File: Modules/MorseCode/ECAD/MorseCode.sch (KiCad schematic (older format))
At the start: 20 parts, among them J1 comm_header, J2 prog_header, SW1 Left, SW2 Right, SW3 Submit, U1 ATmega328-PU, U2 KCSC02-105, U3 KCSC02-105, U4 MAX7219, U5 KCSC02-105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

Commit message: Added polyfuses to all modules
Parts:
- added F1: Polyfuse, symbol Device:Polyfuse
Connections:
- net labels added: UVCC
- wire segments 126 -> 128
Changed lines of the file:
@@
 EESchema Schematic File Version 4
 LIBS:MorseCode-cache
-LIBS:Memory-cache
 EELAYER 29 0
 EELAYER END
@@
 L power:VCC #PWR01
 U 1 1 5F5DC5B2
-P 1400 3350
-F 0 "#PWR01" H 1400 3200 50  0001 C CNN
-F 1 "VCC" V 1418 3477 50  0000 L CNN
-F 2 "" H 1400 3350 50  0001 C CNN
-F 3 "" H 1400 3350 50  0001 C CNN
-	1    1400 3350
-	0    -1   -1   0
-$EndComp
-$Comp
-L power:VCC #PWR03
-U 1 1 5F5DD568
-P 1400 3950
-F 0 "#PWR03" H 1400 3800 50  0001 C CNN
-F 1 "VCC" V 1418 4077 50  0000 L CNN
-F 2 "" H 1400 3950 50  0001 C CNN
-F 3 "" H 1400 3950 50  0001 C CNN
-	1    1400 3950
-	0    -1   -1   0
+P 2250 3050
+F 0 "#PWR01" H 2250 2900 50  0001 C CNN
+F 1 "VCC" V 2268 3177 50  0000 L CNN
+F 2 "" H 2250 3050 50  0001 C CNN
+F 3 "" H 2250 3050 50  0001 C CNN
+	1    2250 3050
+	0    1    1    0
 $EndComp
 $Comp
@@
 Wire Wire Line
 	4850 2450 4400 2450
+$Comp
+L Device:Polyfuse F1
+U 1 1 5F923195
+P 2000 3050
+F 0 "F1" V 1775 3050 50  0000 C CNN
+F 1 "Polyfuse" V 1866 3050 50  0000 C CNN
+F 2 "" H 2050 2850 50  0001 L CNN
+F 3 "~" H 2000 3050 50  0001 C CNN
+	1    2000 3050
+	0    1    1    0
+$EndComp
+Text Label 1400 3950 2    50   ~ 0
+UVCC
+Text Label 1400 3350 2    50   ~ 0
+UVCC
+Text Label 1750 3050 2    50   ~ 0
+UVCC
+Wire Wire Line
+	1750 3050 1850 3050
+Wire Wire Line
+	2150 3050 2250 3050
 $EndSCHEMATC

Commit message: KiCad version update
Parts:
- U1: symbol MCU_Microchip_ATmega:ATmega328-PU -> MorseCode-rescue:ATmega328-PU-MCU_Microchip_ATmega
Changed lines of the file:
@@
 EESchema Schematic File Version 4
-LIBS:MorseCode-cache
-EELAYER 29 0
+EELAYER 30 0
 EELAYER END
 $Descr A4 11693 8268
@@
 $EndDescr
 $Comp
-L MCU_Microchip_ATmega:ATmega328-PU U1
+L MorseCode-rescue:ATmega328-PU-MCU_Microchip_ATmega U1
 U 1 1 5F833469
 P 3800 3250

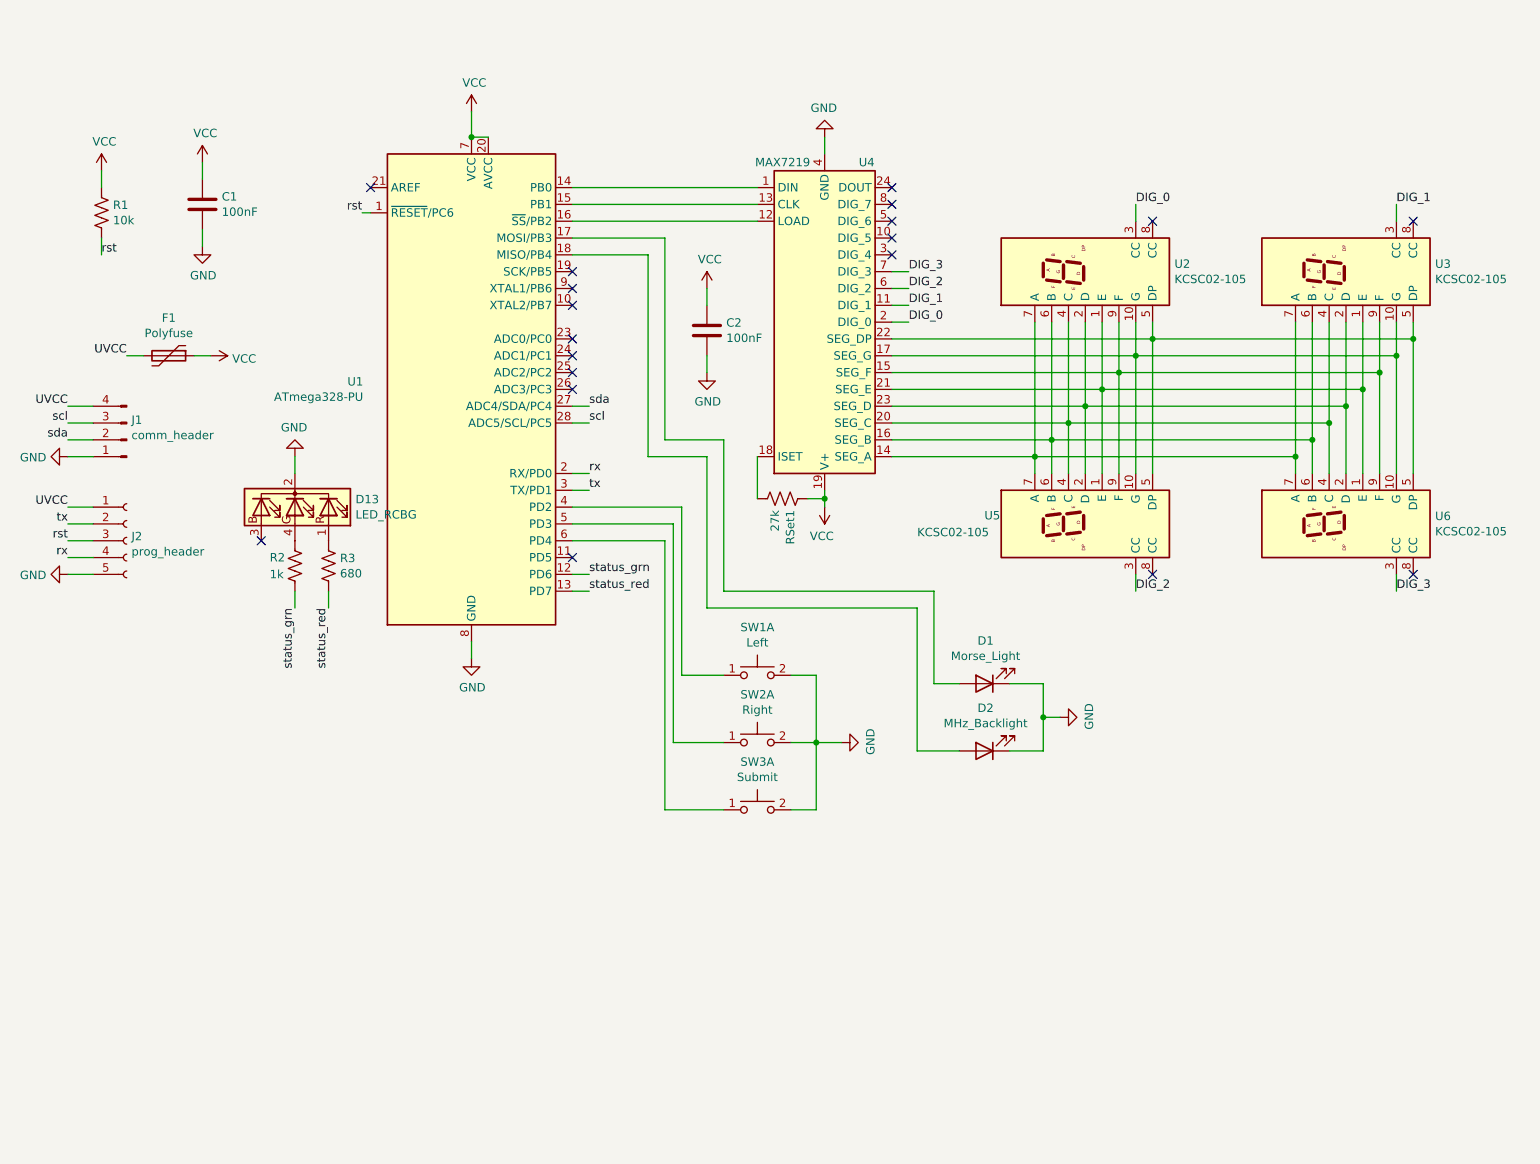
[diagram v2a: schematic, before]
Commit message: MorseCode: Added motor to schematic
This small motor will be used to show frequency with a physical marker
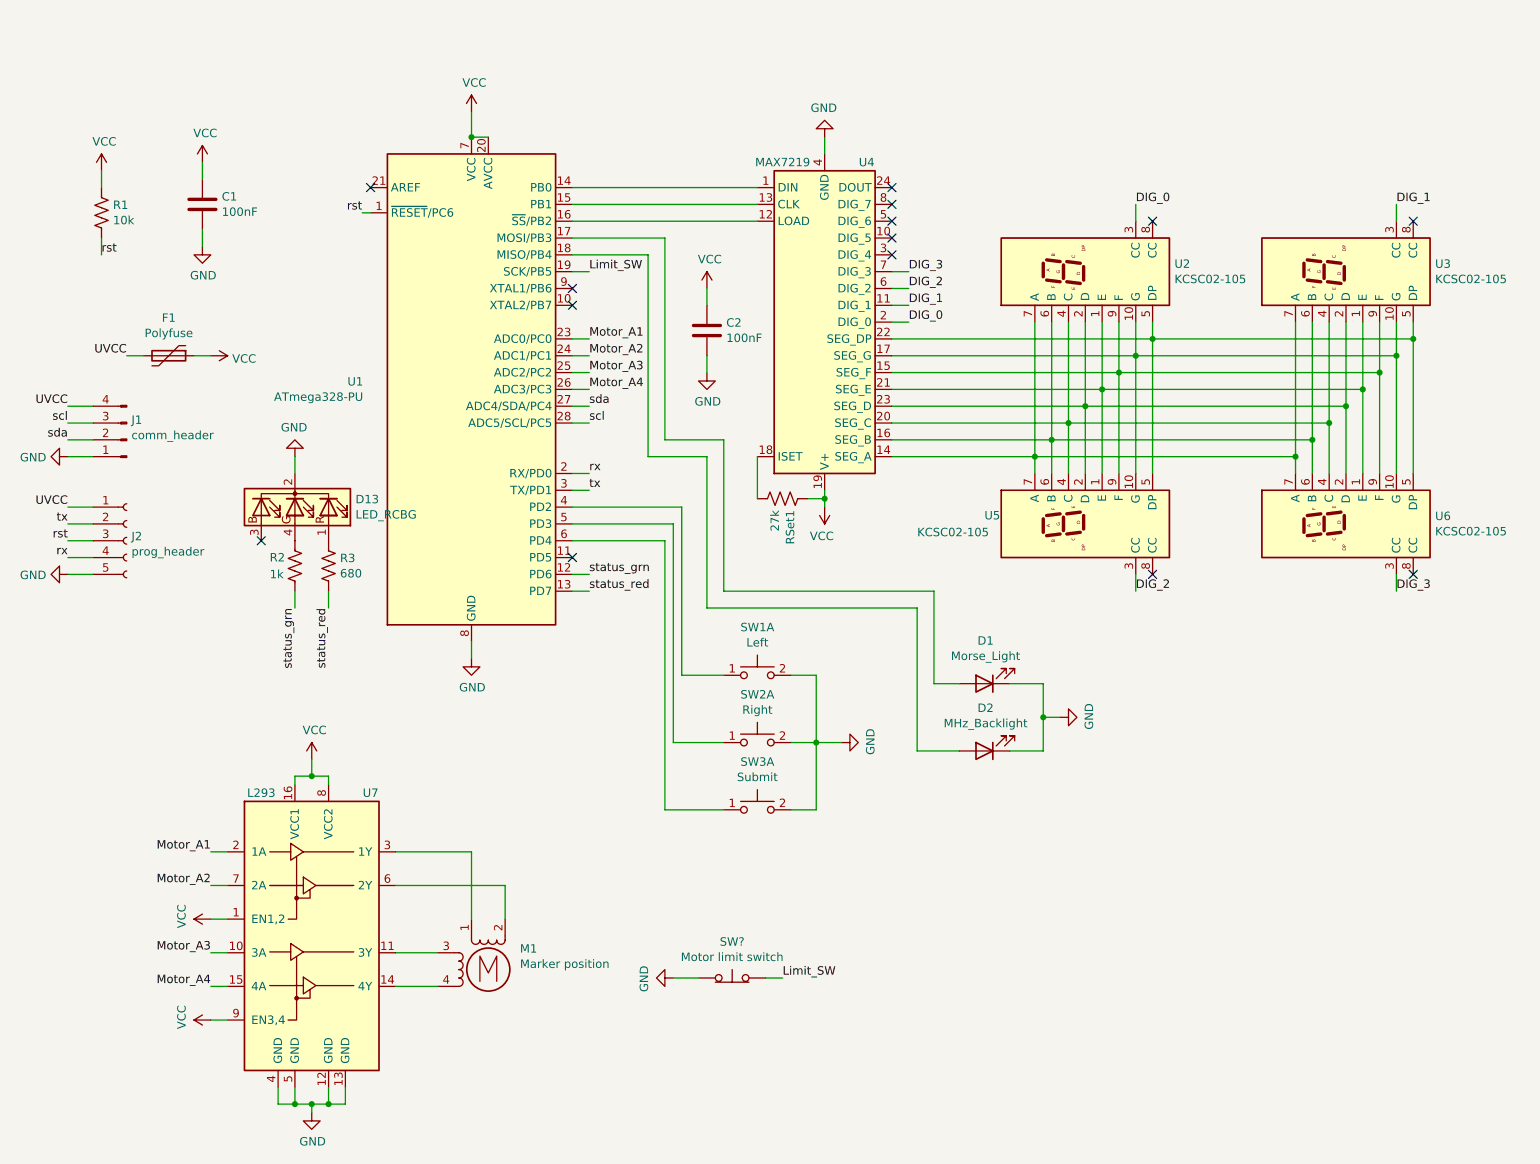
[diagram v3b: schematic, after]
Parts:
- added M1: Marker position, symbol Motor:Stepper_Motor_bipolar
- added SW?: Motor limit switch, symbol Switch:SW_Push_Open
- added U7: L293, Package_DIP:DIP-16_W7.62mm, symbol Driver_Motor:L293
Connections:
- net GND: now also SW?.1 (A), U7.12 (GND), U7.13 (GND), U7.4 (GND), U7.5 (GND)
- net VCC: now also U7.1 (EN1,2), U7.16 (VCC1), U7.8 (VCC2), U7.9 (EN3,4)
- net Limit_SW: now reaches U1.19 (SCK/PB5)
- net Limit_SW: now also SW?.2 (B)
- net Motor_A1: now reaches U1.23 (ADC0/PC0)
- net Motor_A1: now also U7.2 (1A)
- net Motor_A2: now reaches U1.24 (ADC1/PC1)
- net Motor_A2: now also U7.7 (2A)
- net Motor_A3: now reaches U1.25 (ADC2/PC2)
- net Motor_A3: now also U7.10 (3A)
- net Motor_A4: now reaches U1.26 (ADC3/PC3)
- net Motor_A4: now also U7.15 (4A)
- new net: M1.3, U7.11 (3Y)
- new net: M1.4, U7.14 (4Y)
- new net: M1.1, U7.3 (1Y)
- new net: M1.2 (-), U7.6 (2Y)
- no-connect marks 19 -> 14
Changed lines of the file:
@@
 Text Label 2950 4550 3    50   ~ 0
 status_red
-NoConn ~ 4400 2550
 NoConn ~ 4400 2650
 NoConn ~ 4400 2750
-NoConn ~ 4400 2950
-NoConn ~ 4400 3050
-NoConn ~ 4400 3150
-NoConn ~ 4400 3250
 $Comp
 L Device:R_US R2
@@
 Wire Wire Line
 	2150 3050 2250 3050
+$Comp
+L Driver_Motor:L293 U7
+U 1 1 60C7C92C
+P 2850 6600
+F 0 "U7" H 3200 7550 50  0000 C CNN
+F 1 "L293" H 2550 7550 50  0000 C CNN
+F 2 "Package_DIP:DIP-16_W7.62mm" H 3100 5850 50  0001 L CNN
+F 3 "http://www.ti.com/lit/ds/symlink/l293.pdf" H 2550 7300 50  0001 C CNN
+	1    2850 6600
+	1    0    0    -1
+$EndComp
+$Comp
+L power:GND #PWR019
+U 1 1 60C82B18
+P 2850 7550
+F 0 "#PWR019" H 2850 7300 50  0001 C CNN
+F 1 "GND" H 2855 7377 50  0000 C CNN
+F 2 "" H 2850 7550 50  0001 C CNN
+F 3 "" H 2850 7550 50  0001 C CNN
+	1    2850 7550
+	1    0    0    -1
+$EndComp
+$Comp
+L power:VCC #PWR018
+U 1 1 60C8344A
+P 2850 5450
+F 0 "#PWR018" H 2850 5300 50  0001 C CNN
+F 1 "VCC" H 2867 5623 50  0000 C CNN
+F 2 "" H 2850 5450 50  0001 C CNN
+F 3 "" H 2850 5450 50  0001 C CNN
+	1    2850 5450
+	1    0    0    -1
+$EndComp
+Wire Wire Line
+	2750 5600 2750 5550
+Wire Wire Line
+	2750 5550 2850 5550
+Wire Wire Line
+	2850 5550 2850 5450
+Wire Wire Line
+	2950 5600 2950 5550
+Wire Wire Line
+	2950 5550 2850 5550
+Connection ~ 2850 5550
+Wire Wire Line
+	2750 7400 2750 7500
+Wire Wire Line
+	2750 7500 2850 7500
+Wire Wire Line
+	2850 7500 2850 7550
+Wire Wire Line
+	2950 7400 2950 7500
+Wire Wire Line
+	2950 7500 2850 7500
+Connection ~ 2850 7500
+Wire Wire Line
+	3050 7400 3050 7500
+Wire Wire Line
+	3050 7500 2950 7500
+Connection ~ 2950 7500
+Wire Wire Line
+	2650 7400 2650 7500
+Wire Wire Line
+	2650 7500 2750 7500
+Connection ~ 2750 7500
+$Comp
+L Motor:Stepper_Motor_bipolar M1
+U 1 1 60CA94C4
+P 3900 6700
+F 0 "M1" H 4088 6824 50  0000 L CNN
+F 1 "Marker position" H 4088 6733 50  0000 L CNN
+F 2 "" H 3910 6690 50  0001 C CNN
+F 3 "http://www.infineon.com/dgdl/Application-Note-TLE8110EE_driving_UniPolarStepperMotor_V1.1.pdf?fileId=db3a30431be39b97011be5d0aa0a00b0" H 3910 6690 50  0001 C CNN
+	1    3900 6700
+	1    0    0    -1
+$EndComp
+Wire Wire Line
+	3350 6600 3600 6600
+Wire Wire Line
+	3600 6800 3350 6800
+Wire Wire Line
+	3350 6000 3800 6000
+Wire Wire Line
+	3800 6000 3800 6400
+Wire Wire Line
+	3350 6200 4000 6200
+Wire Wire Line
+	4000 6200 4000 6400
+Wire Wire Line
+	4500 2950 4400 2950
+Wire Wire Line
+	4500 3050 4400 3050
+Wire Wire Line
+	4500 3150 4400 3150
+Wire Wire Line
+	4500 3250 4400 3250
+Text Label 4500 2950 0    50   ~ 0
+Motor_A1
+Text Label 4500 3050 0    50   ~ 0
+Motor_A2
+Text Label 4500 3150 0    50   ~ 0
+Motor_A3
+Text Label 4500 3250 0    50   ~ 0
+Motor_A4
+Wire Wire Line
+	2250 6000 2350 6000
+Wire Wire Line
+	2250 6200 2350 6200
+Wire Wire Line
+	2250 6600 2350 6600
+Wire Wire Line
+	2250 6800 2350 6800
+Text Label 2250 6800 2    50   ~ 0
+Motor_A4
+Text Label 2250 6600 2    50   ~ 0
+Motor_A3
+Text Label 2250 6200 2    50   ~ 0
+Motor_A2
+Text Label 2250 6000 2    50   ~ 0
+Motor_A1
+$Comp
+L power:VCC #PWR017
+U 1 1 60D0045A
+P 2250 7000
+F 0 "#PWR017" H 2250 6850 50  0001 C CNN
+F 1 "VCC" H 2267 7173 50  0000 C CNN
+F 2 "" H 2250 7000 50  0001 C CNN
+F 3 "" H 2250 7000 50  0001 C CNN
+	1    2250 7000
+	0    -1   -1   0
+$EndComp
+$Comp
+L power:VCC #PWR03
+U 1 1 60D02180
+P 2250 6400
+F 0 "#PWR03" H 2250 6250 50  0001 C CNN
+F 1 "VCC" H 2267 6573 50  0000 C CNN
+F 2 "" H 2250 6400 50  0001 C CNN
+F 3 "" H 2250 6400 50  0001 C CNN
+	1    2250 6400
+	0    -1   -1   0
+$EndComp
+Wire Wire Line
+	2250 6400 2350 6400
+Wire Wire Line
+	2350 7000 2250 7000
+$Comp
+L Switch:SW_Push_Open SW?
+U 1 1 60D12947
+P 5350 6750
+F 0 "SW?" H 5350 6965 50  0000 C CNN
+F 1 "Motor limit switch" H 5350 6874 50  0000 C CNN
+F 2 "" H 5350 6950 50  0001 C CNN
+F 3 "~" H 5350 6950 50  0001 C CNN
+	1    5350 6750
+	1    0    0    -1
+$EndComp
+$Comp
+L power:GND #PWR?
+U 1 1 60D142A4
+P 5000 6750
+F 0 "#PWR?" H 5000 6500 50  0001 C CNN
+F 1 "GND" H 5005 6577 50  0000 C CNN
+F 2 "" H 5000 6750 50  0001 C CNN
+F 3 "" H 5000 6750 50  0001 C CNN
+	1    5000 6750
+	0    1    1    0
+$EndComp
+Wire Wire Line
+	5000 6750 5150 6750
+Wire Wire Line
+	5650 6750 5550 6750
+Text Label 5650 6750 0    50   ~ 0
+Limit_SW
+Text Label 4500 2550 0    50   ~ 0
+Limit_SW
+Wire Wire Line
+	4500 2550 4400 2550
 $EndSCHEMATC

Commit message: Update a bunch of stuff
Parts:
- removed SW?: Motor limit switch, symbol Switch:SW_Push_Open
- added R4: 10k, symbol Device:R_US
- added SW4: SW_Push_Dual, symbol Switch:SW_Push_Dual
- added SW5, SW6: SW_Push_SPDT, symbol Switch:SW_Push_SPDT
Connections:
- net GND: now also SW4.2, SW5.1 (A), SW6.1 (A)
- net Limit_SW: now also SW5.2 (B), SW6.2 (B)
- net VCC: now also R4.1, SW5.3 (C), SW6.3 (C); no longer U7.1 (EN1,2), U7.9 (EN3,4)
- net rst: now also SW4.1
- net Motor_EN: now reaches U1.11 (PD5)
- net Motor_EN: now also U7.1 (EN1,2), U7.9 (EN3,4), R4.2
- no-connect marks 14 -> 15
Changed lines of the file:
@@
 Wire Wire Line
 	4400 4150 4950 4150
-NoConn ~ 4400 4250
 $Comp
 L power:GND #PWR016
@@
 Text Label 2250 6000 2    50   ~ 0
 Motor_A1
-$Comp
-L power:VCC #PWR017
-U 1 1 60D0045A
-P 2250 7000
-F 0 "#PWR017" H 2250 6850 50  0001 C CNN
-F 1 "VCC" H 2267 7173 50  0000 C CNN
-F 2 "" H 2250 7000 50  0001 C CNN
-F 3 "" H 2250 7000 50  0001 C CNN
-	1    2250 7000
-	0    -1   -1   0
-$EndComp
-$Comp
-L power:VCC #PWR03
-U 1 1 60D02180
-P 2250 6400
-F 0 "#PWR03" H 2250 6250 50  0001 C CNN
-F 1 "VCC" H 2267 6573 50  0000 C CNN
-F 2 "" H 2250 6400 50  0001 C CNN
-F 3 "" H 2250 6400 50  0001 C CNN
-	1    2250 6400
-	0    -1   -1   0
-$EndComp
-Wire Wire Line
-	2250 6400 2350 6400
-Wire Wire Line
-	2350 7000 2250 7000
-$Comp
-L Switch:SW_Push_Open SW?
-U 1 1 60D12947
-P 5350 6750
-F 0 "SW?" H 5350 6965 50  0000 C CNN
-F 1 "Motor limit switch" H 5350 6874 50  0000 C CNN
-F 2 "" H 5350 6950 50  0001 C CNN
-F 3 "~" H 5350 6950 50  0001 C CNN
-	1    5350 6750
-	1    0    0    -1
-$EndComp
-$Comp
-L power:GND #PWR?
-U 1 1 60D142A4
-P 5000 6750
-F 0 "#PWR?" H 5000 6500 50  0001 C CNN
-F 1 "GND" H 5005 6577 50  0000 C CNN
-F 2 "" H 5000 6750 50  0001 C CNN
-F 3 "" H 5000 6750 50  0001 C CNN
-	1    5000 6750
-	0    1    1    0
-$EndComp
-Wire Wire Line
-	5000 6750 5150 6750
-Wire Wire Line
-	5650 6750 5550 6750
-Text Label 5650 6750 0    50   ~ 0
-Limit_SW
 Text Label 4500 2550 0    50   ~ 0
 Limit_SW
 Wire Wire Line
 	4500 2550 4400 2550
+$Comp
+L Switch:SW_Push_Dual SW4
+U 1 1 60F94C85
+P 2850 1350
+F 0 "SW4" H 2850 1635 50  0000 C CNN
+F 1 "SW_Push_Dual" H 2850 1544 50  0000 C CNN
+F 2 "" H 2850 1550 50  0001 C CNN
+F 3 "~" H 2850 1550 50  0001 C CNN
+	1    2850 1350
+	1    0    0    -1
+$EndComp
+$Comp
+L power:GND #PWR017
+U 1 1 60F95EC8
+P 3150 1350
+F 0 "#PWR017" H 3150 1100 50  0001 C CNN
+F 1 "GND" H 3155 1177 50  0000 C CNN
+F 2 "" H 3150 1350 50  0001 C CNN
+F 3 "" H 3150 1350 50  0001 C CNN
+	1    3150 1350
+	0    -1   -1   0
+$EndComp
+Text Label 2550 1350 2    50   ~ 0
+rst
+Wire Wire Line
+	2550 1350 2650 1350
+Wire Wire Line
+	3050 1350 3150 1350
+NoConn ~ 3050 1550
+NoConn ~ 2650 1550
+Wire Wire Line
+	2350 6400 1700 6400
+Wire Wire Line
+	1700 6400 1700 6700
+Wire Wire Line
+	1700 7000 2350 7000
+Wire Wire Line
+	1500 6700 1600 6700
+Connection ~ 1700 6700
+Wire Wire Line
+	1700 6700 1700 7000
+Text Label 1500 6700 2    50   ~ 0
+Motor_EN
+$Comp
+L power:GND #PWR022
+U 1 1 60FBA187
+P 5900 7050
+F 0 "#PWR022" H 5900 6800 50  0001 C CNN
+F 1 "GND" H 5905 6877 50  0000 C CNN
+F 2 "" H 5900 7050 50  0001 C CNN
+F 3 "" H 5900 7050 50  0001 C CNN
+	1    5900 7050
+	0    -1   -1   0
+$EndComp
+Wire Wire Line
+	5900 7050 5800 7050
+$Comp
+L Switch:SW_Push_SPDT SW6
+U 1 1 60FCEC60
+P 5600 7150
+F 0 "SW6" H 5600 7435 50  0000 C CNN
+F 1 "SW_Push_SPDT" H 5600 7344 50  0000 C CNN
+F 2 "" H 5600 7150 50  0001 C CNN
+F 3 "~" H 5600 7150 50  0001 C CNN
+	1    5600 7150
+	1    0    0    -1
+$EndComp
+Text Label 5300 7150 2    50   ~ 0
+Limit_SW
+$Comp
+L Device:R_US R4
+U 1 1 61046196
+P 1600 6450
+F 0 "R4" H 1450 6500 50  0000 L CNN
+F 1 "10k" H 1400 6400 50  0000 L CNN
+F 2 "" V 1640 6440 50  0001 C CNN
+F 3 "~" H 1600 6450 50  0001 C CNN
+	1    1600 6450
+	1    0    0    -1
+$EndComp
+Wire Wire Line
+	1600 6700 1600 6600
+Connection ~ 1600 6700
+Wire Wire Line
+	1600 6700 1700 6700
+$Comp
+L power:VCC #PWR03
+U 1 1 61057D44
+P 1600 6200
+F 0 "#PWR03" H 1600 6050 50  0001 C CNN
+F 1 "VCC" H 1617 6373 50  0000 C CNN
+F 2 "" H 1600 6200 50  0001 C CNN
+F 3 "" H 1600 6200 50  0001 C CNN
+	1    1600 6200
+	1    0    0    -1
+$EndComp
+Wire Wire Line
+	1600 6200 1600 6300
+$Comp
+L power:VCC #PWR023
+U 1 1 61075F13
+P 5900 7250
+F 0 "#PWR023" H 5900 7100 50  0001 C CNN
+F 1 "VCC" H 5917 7423 50  0000 C CNN
+F 2 "" H 5900 7250 50  0001 C CNN
+F 3 "" H 5900 7250 50  0001 C CNN
+	1    5900 7250
+	0    1    1    0
+$EndComp
+Wire Wire Line
+	4500 4250 4400 4250
+Text Label 4500 4250 0    50   ~ 0
+Motor_EN
+Wire Wire Line
+	5400 7150 5300 7150
+Wire Wire Line
+	5900 7250 5800 7250
+$Comp
+L power:GND #PWR020
+U 1 1 6111A8F1
+P 5900 6400
+F 0 "#PWR020" H 5900 6150 50  0001 C CNN
+F 1 "GND" H 5905 6227 50  0000 C CNN
+F 2 "" H 5900 6400 50  0001 C CNN
+F 3 "" H 5900 6400 50  0001 C CNN
+	1    5900 6400
+	0    -1   -1   0
+$EndComp
+Wire Wire Line
+	5900 6400 5800 6400
+$Comp
+L Switch:SW_Push_SPDT SW5
+U 1 1 6111A8F8
+P 5600 6500
+F 0 "SW5" H 5600 6785 50  0000 C CNN
+F 1 "SW_Push_SPDT" H 5600 6694 50  0000 C CNN
+F 2 "" H 5600 6500 50  0001 C CNN
+F 3 "~" H 5600 6500 50  0001 C CNN
+	1    5600 6500
+	1    0    0    -1
+$EndComp
+Text Label 5300 6500 2    50   ~ 0
+Limit_SW
+$Comp
+L power:VCC #PWR021
+U 1 1 6111A8FF
+P 5900 6600
+F 0 "#PWR021" H 5900 6450 50  0001 C CNN
+F 1 "VCC" H 5917 6773 50  0000 C CNN
+F 2 "" H 5900 6600 50  0001 C CNN
+F 3 "" H 5900 6600 50  0001 C CNN
+	1    5900 6600
+	0    1    1    0
+$EndComp
+Wire Wire Line
+	5400 6500 5300 6500
+Wire Wire Line
+	5900 6600 5800 6600
 $EndSCHEMATC
